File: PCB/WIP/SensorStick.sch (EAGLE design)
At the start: 87 parts, among them CON2 B6B-ZR, CON3 B6B-ZR, U1 TPD4F003DQDR, U10 LIS3MDLTR, U11 LIS3MDLTR, U2 BMI088, U3 BMI088, U4 BMI088, U5 STM32H743ZIT6, U9 LIS3MDLTR, Y1 ECS-TXO-3225MV-400-TR

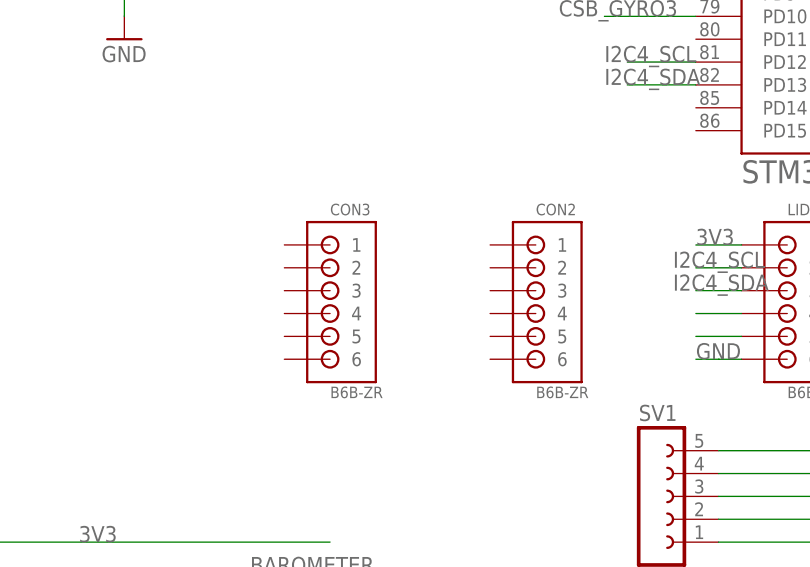
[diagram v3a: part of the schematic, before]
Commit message: all jsts added, board mostly laid out, working on connections now
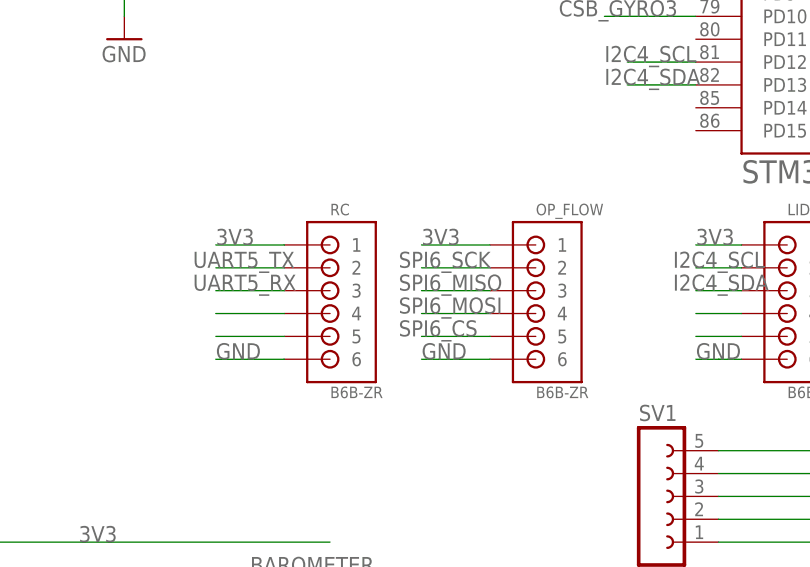
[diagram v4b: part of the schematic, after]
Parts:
- renumbered CON2 to OP_FLOW, CON3 to RC
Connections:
- new net N$18: RC.4
- new net N$19: RC.5
- net 3V3: now also OP_FLOW.1, RC.1
- net GND: now also OP_FLOW.6, RC.6
- net SPI6_CS: now also OP_FLOW.5
- net SPI6_MISO: now also OP_FLOW.3
- net SPI6_MOSI: now also OP_FLOW.4
- net SPI6_SCK: now also OP_FLOW.2
- net UART5_RX: now also RC.3
- net UART5_TX: now also RC.2
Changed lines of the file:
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@@
 <part name="R21" library="ce-capstone" deviceset="RT0402FRE07220RL" device=""/>
 <part name="LIDAR" library="jst" deviceset="B6B-ZR" device=""/>
-<part name="CON2" library="jst" deviceset="B6B-ZR" device=""/>
-<part name="CON3" library="jst" deviceset="B6B-ZR" device=""/>
+<part name="OP_FLOW" library="jst" deviceset="B6B-ZR" device=""/>
+<part name="RC" library="jst" deviceset="B6B-ZR" device=""/>
 </parts>
 <sheets>
@@
 <attribute name="VALUE" x="119.38" y="99.822" size="1.27" layer="96"/>
 </instance>
-<instance part="CON2" gate="G$1" x="91.44" y="116.84" smashed="yes">
+<instance part="OP_FLOW" gate="G$1" x="91.44" y="116.84" smashed="yes">
 <attribute name="NAME" x="91.44" y="120.142" size="1.27" layer="95"/>
 <attribute name="VALUE" x="91.44" y="99.822" size="1.27" layer="96"/>
 </instance>
-<instance part="CON3" gate="G$1" x="68.58" y="116.84" smashed="yes">
+<instance part="RC" gate="G$1" x="68.58" y="116.84" smashed="yes">
 <attribute name="NAME" x="68.58" y="120.142" size="1.27" layer="95"/>
 <attribute name="VALUE" x="68.58" y="99.822" size="1.27" layer="96"/>
@@
 <label x="109.22" y="116.84" size="1.778" layer="95"/>
 <pinref part="LIDAR" gate="G$1" pin="1"/>
+</segment>
+<segment>
+<pinref part="OP_FLOW" gate="G$1" pin="1"/>
+<wire x1="86.36" y1="116.84" x2="78.74" y2="116.84" width="0.1524" layer="91"/>
+<label x="78.74" y="116.84" size="1.778" layer="95"/>
+</segment>
+<segment>
+<pinref part="RC" gate="G$1" pin="1"/>
+<wire x1="63.5" y1="116.84" x2="55.88" y2="116.84" width="0.1524" layer="91"/>
+<label x="55.88" y="116.84" size="1.778" layer="95"/>
 </segment>
 </net>
@@
 <label x="109.22" y="104.14" size="1.778" layer="95"/>
 </segment>
+<segment>
+<pinref part="OP_FLOW" gate="G$1" pin="6"/>
+<wire x1="86.36" y1="104.14" x2="78.74" y2="104.14" width="0.1524" layer="91"/>
+<label x="78.74" y="104.14" size="1.778" layer="95"/>
+</segment>
+<segment>
+<pinref part="RC" gate="G$1" pin="6"/>
+<wire x1="63.5" y1="104.14" x2="55.88" y2="104.14" width="0.1524" layer="91"/>
+<label x="55.88" y="104.14" size="1.778" layer="95"/>
+</segment>
 </net>
 <net name="I2C2_SCL" class="0">
@@
 <label x="2.54" y="281.94" size="1.778" layer="95"/>
 </segment>
+<segment>
+<pinref part="OP_FLOW" gate="G$1" pin="2"/>
+<wire x1="86.36" y1="114.3" x2="78.74" y2="114.3" width="0.1524" layer="91"/>
+<label x="76.2" y="114.3" size="1.778" layer="95"/>
+</segment>
 </net>
 <net name="SPI6_MISO" class="0">
@@
 <label x="2.54" y="279.4" size="1.778" layer="95"/>
 </segment>
+<segment>
+<pinref part="OP_FLOW" gate="G$1" pin="3"/>
+<wire x1="86.36" y1="111.76" x2="78.74" y2="111.76" width="0.1524" layer="91"/>
+<label x="76.2" y="111.76" size="1.778" layer="95"/>
+</segment>
 </net>
 <net name="SPI6_MOSI" class="0">
@@
 <wire x1="15.24" y1="276.86" x2="5.08" y2="276.86" width="0.1524" layer="91"/>
 <label x="2.54" y="276.86" size="1.778" layer="95"/>
+</segment>
+<segment>
+<pinref part="OP_FLOW" gate="G$1" pin="4"/>
+<wire x1="86.36" y1="109.22" x2="78.74" y2="109.22" width="0.1524" layer="91"/>
+<label x="76.2" y="109.22" size="1.778" layer="95"/>
 </segment>
 </net>
@@
 <label x="198.12" y="175.26" size="1.778" layer="95"/>
 </segment>
+<segment>
+<pinref part="OP_FLOW" gate="G$1" pin="5"/>
+<wire x1="86.36" y1="106.68" x2="78.74" y2="106.68" width="0.1524" layer="91"/>
+<label x="76.2" y="106.68" size="1.778" layer="95"/>
+</segment>
 </net>
 <net name="I2C4_SCL" class="0">
@@
 <pinref part="U5" gate="G$2" pin="PB5"/>
 </segment>
+<segment>
+<pinref part="RC" gate="G$1" pin="3"/>
+<wire x1="63.5" y1="111.76" x2="55.88" y2="111.76" width="0.1524" layer="91"/>
+<label x="53.34" y="111.76" size="1.778" layer="95"/>
+</segment>
 </net>
 <net name="UART5_TX" class="0">
@@
 <label x="127" y="238.76" size="1.778" layer="95"/>
 <pinref part="U5" gate="G$2" pin="PB6"/>
+</segment>
+<segment>
+<pinref part="RC" gate="G$1" pin="2"/>
+<wire x1="63.5" y1="114.3" x2="55.88" y2="114.3" width="0.1524" layer="91"/>
+<label x="53.34" y="114.3" size="1.778" layer="95"/>
 </segment>
 </net>
@@
 </segment>
 </net>
+<net name="N$18" class="0">
+<segment>
+<pinref part="RC" gate="G$1" pin="4"/>
+<wire x1="63.5" y1="109.22" x2="55.88" y2="109.22" width="0.1524" layer="91"/>
+</segment>
+</net>
+<net name="N$19" class="0">
+<segment>
+<pinref part="RC" gate="G$1" pin="5"/>
+<wire x1="63.5" y1="106.68" x2="55.88" y2="106.68" width="0.1524" layer="91"/>
+</segment>
+</net>

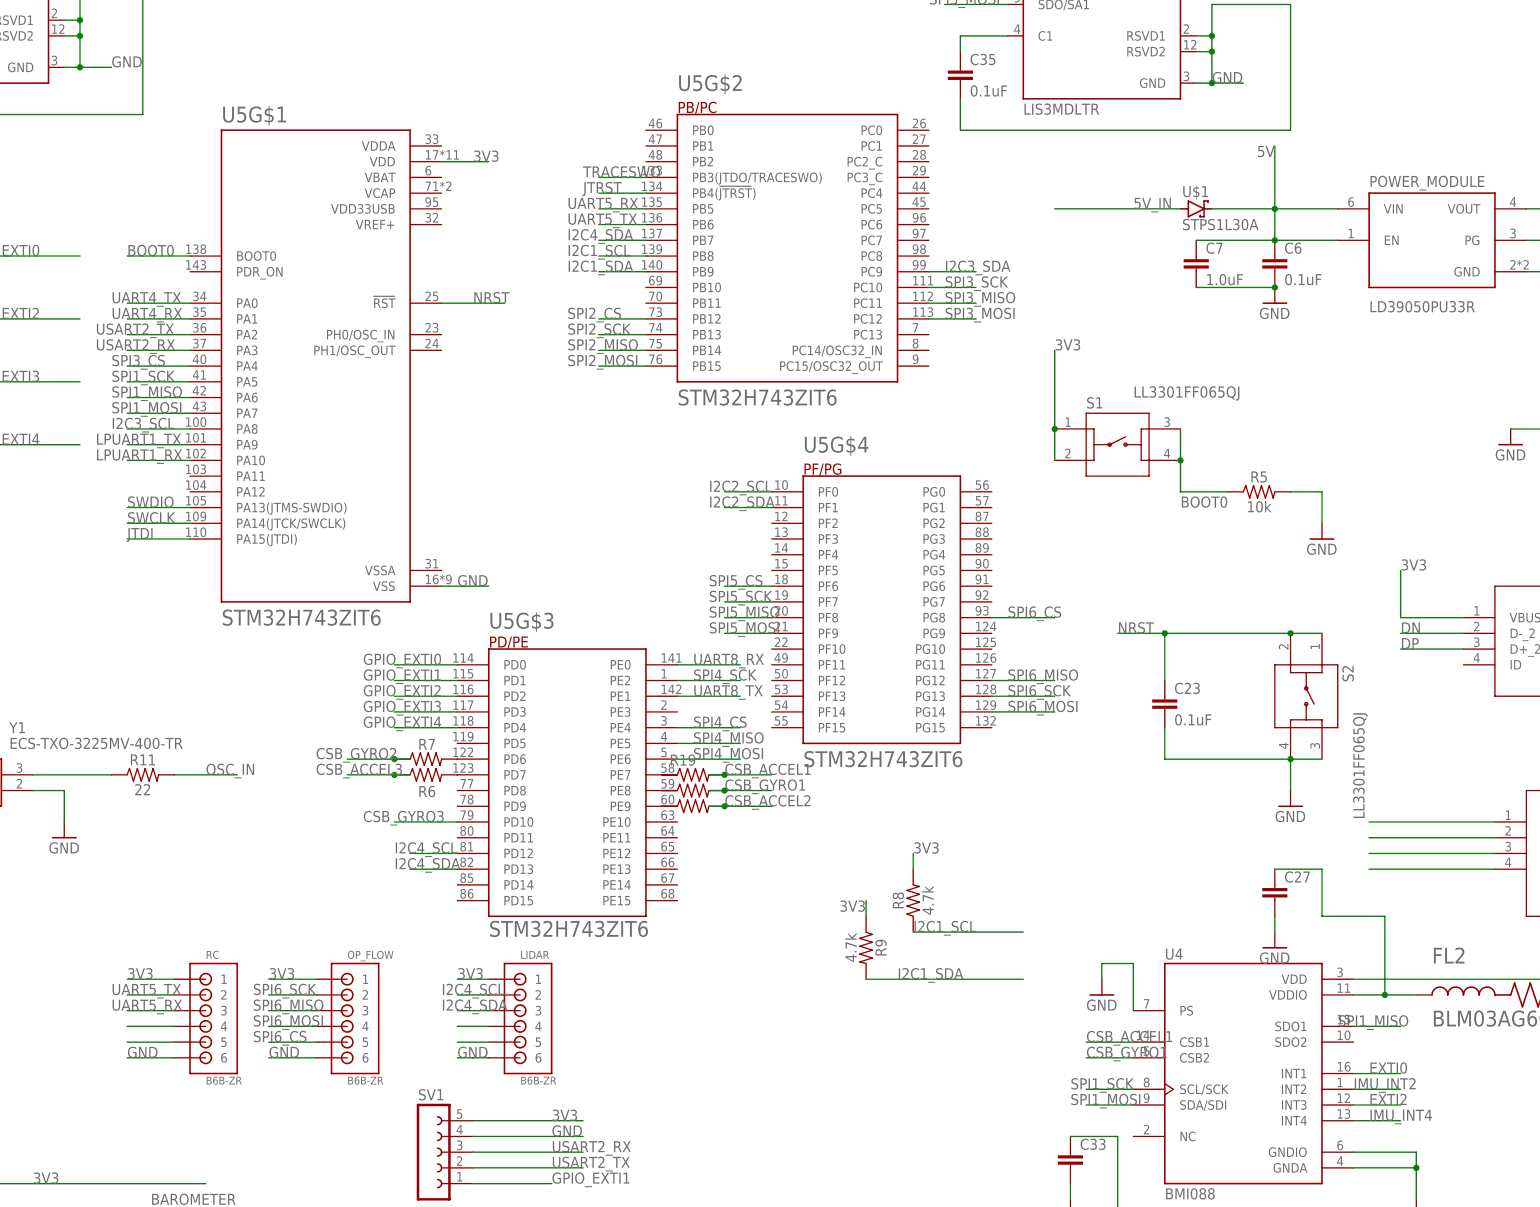
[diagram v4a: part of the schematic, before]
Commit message: some minor changes with VDD, VBAT connections
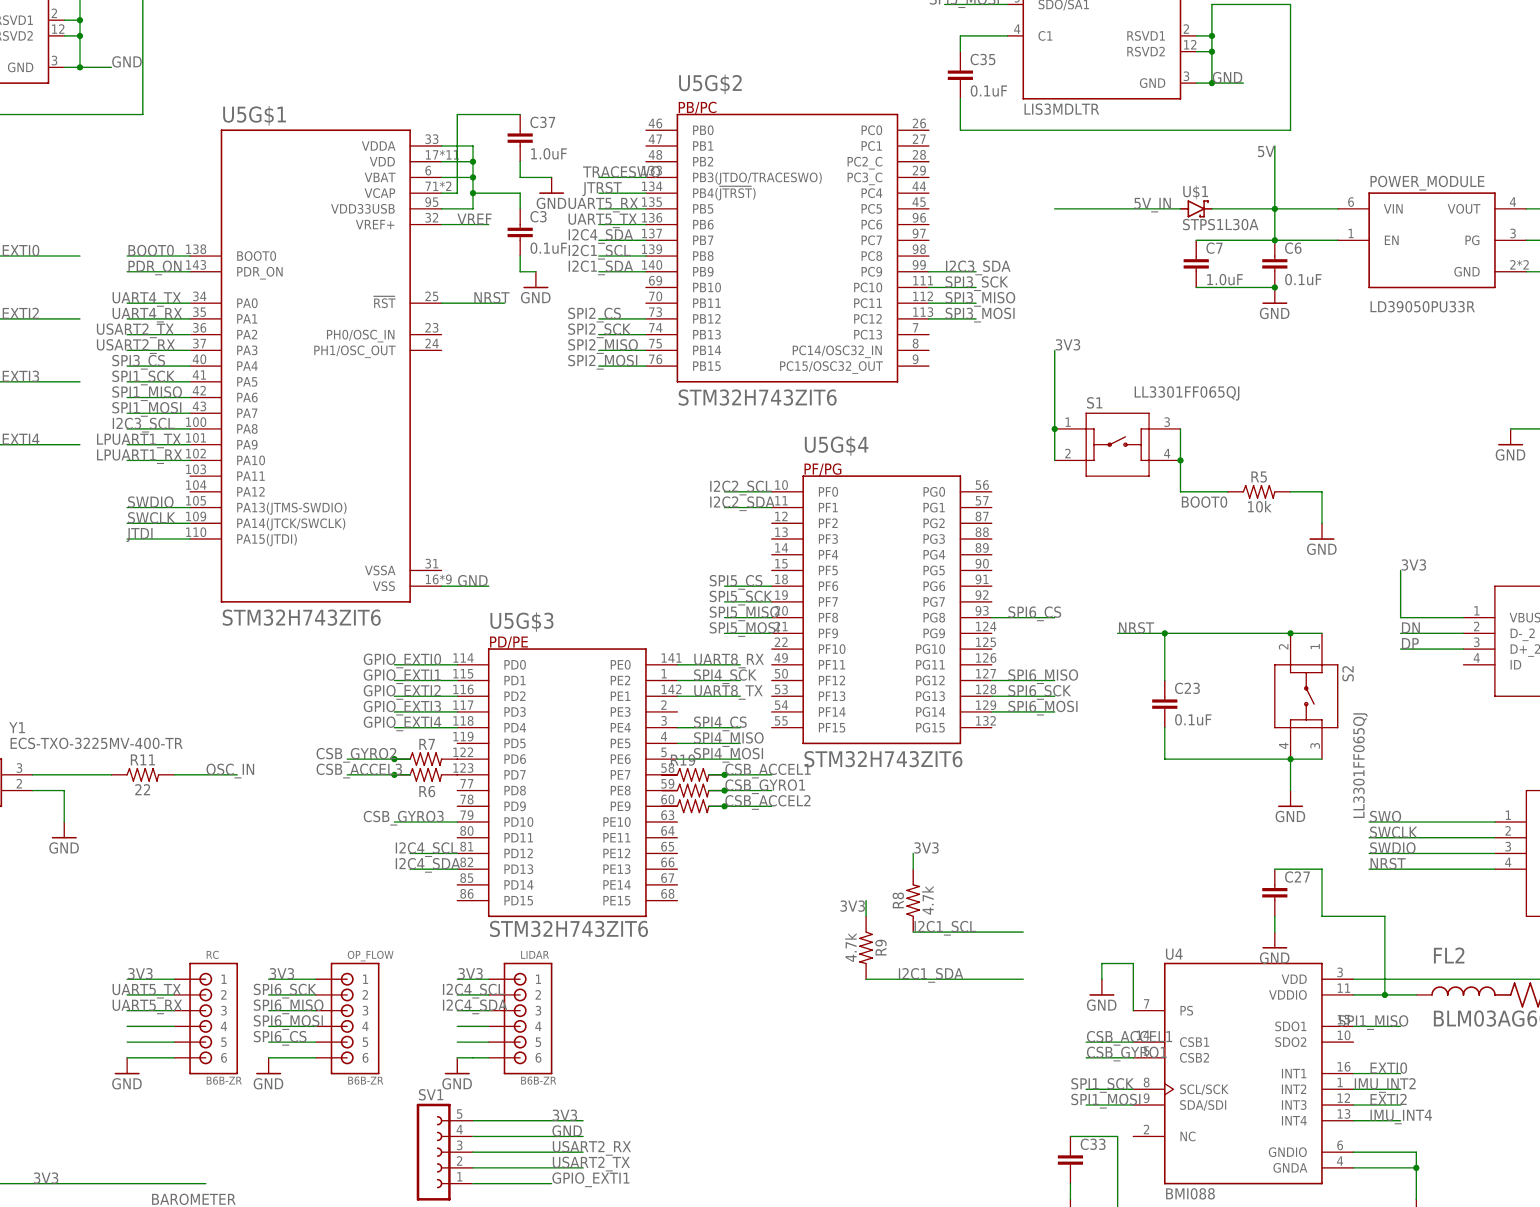
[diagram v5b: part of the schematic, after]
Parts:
- added C3: 0.1uF, capacitor-wima:C2.5/4
- added C37: 1.0uF, SparkFun-Capacitors:1.0UF-0805-25V-10%
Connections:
- removed net NRST1: U1.CH4_IN
- new net N$12: C37.1, U5G$1.VCAP
- new net PDR_ON: U5G$1.PDR_ON
- net 3V3: now also C3.1, U5G$1.VBAT, U5G$1.VDD33USB, U5G$1.VDDA
- net GND: now also C3.2, C37.2
- net NRST: now also U1.CH4_IN
- net VREF: now also U5G$1.VREF+
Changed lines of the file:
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@@
 <part name="OP_FLOW" library="jst" deviceset="B6B-ZR" device=""/>
 <part name="RC" library="jst" deviceset="B6B-ZR" device=""/>
+<part name="C3" library="capacitor-wima" library_urn="urn:adsk.eagle:library:116" deviceset="C" device="2.5/4" package3d_urn="urn:adsk.eagle:package:5408/1" value="0.1uF"/>
+<part name="C37" library="SparkFun-Capacitors" library_urn="urn:adsk.eagle:library:510" deviceset="1.0UF" device="-0805-25V-10%" package3d_urn="urn:adsk.eagle:package:37429/1" value="1.0uF"/>
+<part name="GND8" library="supply1" library_urn="urn:adsk.eagle:library:371" deviceset="GND" device=""/>
+<part name="GND32" library="supply1" library_urn="urn:adsk.eagle:library:371" deviceset="GND" device=""/>
+<part name="GND43" library="supply1" library_urn="urn:adsk.eagle:library:371" deviceset="GND" device=""/>
+<part name="GND44" library="supply1" library_urn="urn:adsk.eagle:library:371" deviceset="GND" device=""/>
+<part name="GND45" library="supply1" library_urn="urn:adsk.eagle:library:371" deviceset="GND" device=""/>
 </parts>
 <sheets>
@@
 <attribute name="NAME" x="68.58" y="120.142" size="1.27" layer="95"/>
 <attribute name="VALUE" x="68.58" y="99.822" size="1.27" layer="96"/>
+</instance>
+<instance part="C3" gate="G$1" x="119.38" y="238.76" smashed="yes">
+<attribute name="NAME" x="120.904" y="239.141" size="1.778" layer="95"/>
+<attribute name="VALUE" x="120.904" y="234.061" size="1.778" layer="96"/>
+</instance>
+<instance part="C37" gate="G$1" x="119.38" y="251.46" smashed="yes">
+<attribute name="NAME" x="120.904" y="254.381" size="1.778" layer="95" font="vector"/>
+<attribute name="VALUE" x="120.904" y="249.301" size="1.778" layer="96" font="vector"/>
+</instance>
+<instance part="GND8" gate="1" x="124.46" y="243.84" smashed="yes">
+<attribute name="VALUE" x="121.92" y="241.3" size="1.778" layer="96"/>
+</instance>
+<instance part="GND32" gate="1" x="121.92" y="228.6" smashed="yes">
+<attribute name="VALUE" x="119.38" y="226.06" size="1.778" layer="96"/>
+</instance>
+<instance part="GND43" gate="1" x="55.88" y="101.6" smashed="yes">
+<attribute name="VALUE" x="53.34" y="99.06" size="1.778" layer="96"/>
+</instance>
+<instance part="GND44" gate="1" x="109.22" y="101.6" smashed="yes">
+<attribute name="VALUE" x="106.68" y="99.06" size="1.778" layer="96"/>
+</instance>
+<instance part="GND45" gate="1" x="78.74" y="101.6" smashed="yes">
+<attribute name="VALUE" x="76.2" y="99.06" size="1.778" layer="96"/>
 </instance>
 </instances>
@@
 <segment>
 <pinref part="U5" gate="G$1" pin="VDD"/>
-<wire x1="106.68" y1="248.92" x2="114.3" y2="248.92" width="0.1524" layer="91"/>
-<label x="111.76" y="248.92" size="1.778" layer="95"/>
+<wire x1="106.68" y1="248.92" x2="111.76" y2="248.92" width="0.1524" layer="91"/>
+<pinref part="U5" gate="G$1" pin="VDDA"/>
+<wire x1="106.68" y1="251.46" x2="111.76" y2="251.46" width="0.1524" layer="91"/>
+<wire x1="111.76" y1="251.46" x2="111.76" y2="248.92" width="0.1524" layer="91"/>
+<pinref part="U5" gate="G$1" pin="VBAT"/>
+<wire x1="111.76" y1="248.92" x2="111.76" y2="246.38" width="0.1524" layer="91"/>
+<wire x1="111.76" y1="246.38" x2="106.68" y2="246.38" width="0.1524" layer="91"/>
+<junction x="111.76" y="248.92"/>
+<pinref part="U5" gate="G$1" pin="VDD33USB"/>
+<wire x1="111.76" y1="246.38" x2="111.76" y2="243.84" width="0.1524" layer="91"/>
+<wire x1="111.76" y1="243.84" x2="111.76" y2="241.3" width="0.1524" layer="91"/>
+<wire x1="111.76" y1="241.3" x2="106.68" y2="241.3" width="0.1524" layer="91"/>
+<junction x="111.76" y="246.38"/>
+<wire x1="111.76" y1="243.84" x2="119.38" y2="243.84" width="0.1524" layer="91"/>
+<junction x="111.76" y="243.84"/>
+<wire x1="119.38" y1="243.84" x2="119.38" y2="241.3" width="0.1524" layer="91"/>
+<pinref part="C3" gate="G$1" pin="1"/>
 </segment>
 <segment>
@@
 <wire x1="114.3" y1="104.14" x2="111.76" y2="104.14" width="0.1524" layer="91"/>
 <wire x1="109.22" y1="104.14" x2="111.76" y2="104.14" width="0.1524" layer="91"/>
-<label x="109.22" y="104.14" size="1.778" layer="95"/>
+<pinref part="GND44" gate="1" pin="GND"/>
 </segment>
 <segment>
 <pinref part="OP_FLOW" gate="G$1" pin="6"/>
 <wire x1="86.36" y1="104.14" x2="78.74" y2="104.14" width="0.1524" layer="91"/>
-<label x="78.74" y="104.14" size="1.778" layer="95"/>
+<pinref part="GND45" gate="1" pin="GND"/>
 </segment>
 <segment>
 <pinref part="RC" gate="G$1" pin="6"/>
 <wire x1="63.5" y1="104.14" x2="55.88" y2="104.14" width="0.1524" layer="91"/>
-<label x="55.88" y="104.14" size="1.778" layer="95"/>
+<pinref part="GND43" gate="1" pin="GND"/>
+</segment>
+<segment>
+<pinref part="C3" gate="G$1" pin="2"/>
+<wire x1="119.38" y1="233.68" x2="119.38" y2="231.14" width="0.1524" layer="91"/>
+<pinref part="GND32" gate="1" pin="GND"/>
+<wire x1="119.38" y1="231.14" x2="121.92" y2="231.14" width="0.1524" layer="91"/>
+</segment>
+<segment>
+<pinref part="C37" gate="G$1" pin="2"/>
+<wire x1="119.38" y1="248.92" x2="119.38" y2="246.38" width="0.1524" layer="91"/>
+<pinref part="GND8" gate="1" pin="GND"/>
+<wire x1="119.38" y1="246.38" x2="124.46" y2="246.38" width="0.1524" layer="91"/>
 </segment>
 </net>
@@
 <pinref part="L1" gate="G$1" pin="2"/>
 </segment>
+<segment>
+<pinref part="U5" gate="G$1" pin="VREF+"/>
+<wire x1="106.68" y1="238.76" x2="114.3" y2="238.76" width="0.1524" layer="91"/>
+<label x="109.22" y="238.76" size="1.778" layer="95"/>
+</segment>
 </net>
 <net name="BOOT0" class="0">
@@
 <label x="111.76" y="226.06" size="1.778" layer="95"/>
 </segment>
+<segment>
+<wire x1="276.86" y1="134.62" x2="256.54" y2="134.62" width="0.1524" layer="91"/>
+<pinref part="U1" gate="A" pin="CH4_IN"/>
+<label x="256.54" y="134.62" size="1.778" layer="95"/>
+</segment>
 </net>
 <net name="DP" class="0">
@@
 </segment>
 </net>
-<net name="NRST1" class="0">
-<segment>
-<wire x1="276.86" y1="134.62" x2="256.54" y2="134.62" width="0.1524" layer="91"/>
-<pinref part="U1" gate="A" pin="CH4_IN"/>
-</segment>
-</net>
 <net name="SWO" class="0">
 <segment>
 <wire x1="276.86" y1="142.24" x2="256.54" y2="142.24" width="0.1524" layer="91"/>
 <pinref part="U1" gate="A" pin="CH1_IN"/>
+<label x="256.54" y="142.24" size="1.778" layer="95"/>
 </segment>
 </net>
@@
 <wire x1="276.86" y1="137.16" x2="256.54" y2="137.16" width="0.1524" layer="91"/>
 <pinref part="U1" gate="A" pin="CH3_IN"/>
+<label x="256.54" y="137.16" size="1.778" layer="95"/>
 </segment>
 <segment>
@@
 <wire x1="276.86" y1="139.7" x2="256.54" y2="139.7" width="0.1524" layer="91"/>
 <pinref part="U1" gate="A" pin="CH2_IN"/>
+<label x="256.54" y="139.7" size="1.778" layer="95"/>
 </segment>
 <segment>
@@
 </segment>
 </net>
+<net name="PDR_ON" class="0">
+<segment>
+<pinref part="U5" gate="G$1" pin="PDR_ON"/>
+<wire x1="66.04" y1="231.14" x2="55.88" y2="231.14" width="0.1524" layer="91"/>
+<label x="55.88" y="231.14" size="1.778" layer="95"/>
+</segment>
+</net>
+<net name="N$12" class="0">
+<segment>
+<pinref part="U5" gate="G$1" pin="VCAP"/>
+<wire x1="106.68" y1="243.84" x2="109.22" y2="243.84" width="0.1524" layer="91"/>
+<wire x1="109.22" y1="243.84" x2="109.22" y2="256.54" width="0.1524" layer="91"/>
+<pinref part="C37" gate="G$1" pin="1"/>
+<wire x1="109.22" y1="256.54" x2="119.38" y2="256.54" width="0.1524" layer="91"/>
+</segment>
+</net>
